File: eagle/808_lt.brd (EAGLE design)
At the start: 100 x 80 mm, 52 parts, among them IC1 TL071P, IC2 TL072P, Q1 2N3904, Q2 2N3906, Q3 2N3904, SW8 MSS42_SW_4PDT

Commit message: routing in low 90s
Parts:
- moved C74 26.7 mm to (7.62, 22.9), turned to 0 degrees
- moved R231 20.7 mm to (34.3, 15.2)
- moved R230 12.5 mm to (39.4, 24.1), turned to 0 degrees
- moved C81 12.0 mm to (78.7, 39.4), turned to 0 degrees
- moved R234 10.5 mm to (74.9, 44.5), turned to 180 degrees
- moved R215 10.2 mm to (33.0, 34.3)
- moved R214 9.92 mm to (25.4, 41.9), turned to 270 degrees
- moved R235 8.98 mm to (87.6, 31.8), turned to 90 degrees
- moved R227 8.03 mm to (43.2, 29.2)
- moved C73 6.35 mm to (33.0, 47.0)
- moved R211 5.24 mm to (21.6, 34.3)
- moved Q2 4.58 mm to (30.5, 40.6), turned to 0 degrees
- moved R216 4.02 mm to (17.8, 22.9)
- moved R219 3.81 mm to (24.1, 50.8)
- moved R229 2.84 mm to (44.5, 36.8)
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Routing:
- net GND: track 0.00 -> 254.7 mm
- net +15V: track 0.00 -> 166.3 mm
- net N$251: track 0.00 -> 138.5 mm
- net N$260: track 0.00 -> 74.7 mm
- net N$253: track 0.00 -> 44.2 mm
- net TRIG: track 0.00 -> 40.8 mm
- net N$264: track 0.00 -> 39.1 mm
- net N$259: track 0.00 -> 33.9 mm
- net N$262: track 0.00 -> 33.7 mm
- net N$273: track 0.00 -> 32.8 mm
- net N$39: track 0.00 -> 32.4 mm
- net N$263: track 0.00 -> 31.1 mm
- net LT: track 0.00 -> 30.9 mm
- net N$257: track 0.00 -> 29.6 mm
- net N$271: track 0.00 -> 22.1 mm
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
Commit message: closer
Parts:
- added OUT_NORM, PINK_NORM: 22-23-2021, con-molex:22-23-2021
- moved R223 31.9 mm to (36.8, 29.2)
- moved C74 26.9 mm to (33.0, 31.8), turned to 270 degrees
- moved R222 21.6 mm to (38.1, 20.3), turned to 90 degrees
- moved C81 18.2 mm to (71.1, 22.9), turned to 270 degrees
- moved R234 16.6 mm to (76.2, 27.9)
- moved C77 14.9 mm to (53.3, 27.9)
- moved C76 9.25 mm to (61.0, 50.8)
- moved R233 8.89 mm to (61.0, 26.7)
- moved C73 8.89 mm to (41.9, 47.0), turned to 0 degrees
- moved R219 8.52 mm to (31.8, 47.0)
- moved C78 8.03 mm to (55.9, 50.8)
- moved D56 8.03 mm to (48.3, 50.8)
- moved R228 8.03 mm to (58.4, 45.7)
- moved R214 7.73 mm to (33.0, 40.6)
- moved Q2 7.62 mm to (38.1, 40.6)
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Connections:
- new net N$3: OUTPUT.P$2, OUT_NORM.1
- new net N$4: PINK_NOISE.P$2, PINK_NORM.1
- net GND: now also OUT_NORM.2, PINK_NORM.2, SW8.P$12; no longer SW8.P$6
- net N$111: now also SW8.P$11; no longer SW8.P$5
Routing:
- net +15V: track 166.3 -> 50.2 mm
- net N$251: track 138.5 -> 31.8 mm
- net GND: track 254.7 -> 357.0 mm
- net -15V: track 2.54 -> 74.1 mm
- net N$264: track 39.1 -> 8.47 mm
- net N$260: track 74.7 -> 44.3 mm
- net N$259: track 33.9 -> 6.96 mm
- net N$273: track 32.8 -> 56.5 mm
- net N$256: track 9.72 -> 29.5 mm
- net N$253: track 44.2 -> 24.8 mm
- net N$111: track 0.00 -> 17.0 mm
- net N$271: track 22.1 -> 8.77 mm
- net N$262: track 33.7 -> 45.1 mm
- net N$257: track 29.6 -> 40.2 mm
- net N$250: track 18.3 -> 8.52 mm
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
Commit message: closer
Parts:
- moved R235 7.41 mm to (81.3, 31.8), turned to 180 degrees
- moved D56 3.81 mm to (48.3, 54.6)
- moved R226 3.81 mm to (49.5, 50.8)
- moved IC1 2.84 mm to (78.7, 38.1)
- moved R224 1.80 mm to (66.0, 34.3)
- moved R225 1.80 mm to (68.6, 45.7)
- moved R228 1.27 mm to (57.1, 45.7)
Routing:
- net GND: track 357.0 -> 0.00 mm
- net -15V: track 74.1 -> 0.00 mm
- net N$273: track 56.5 -> 0.00 mm
- net +15V: track 50.2 -> 0.00 mm
- net N$262: track 45.1 -> 0.00 mm
- net N$260: track 44.3 -> 0.00 mm
- net N$257: track 40.2 -> 0.00 mm
- net TRIG: track 38.3 -> 0.00 mm
- net N$251: track 31.8 -> 0.00 mm
- net N$256: track 29.5 -> 0.00 mm
- net N$263: track 29.2 -> 0.00 mm
- net N$39: track 28.6 -> 0.00 mm
- net LT: track 24.9 -> 0.00 mm
- net N$253: track 24.8 -> 0.00 mm
- net N$111: track 17.0 -> 0.00 mm
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
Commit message: 93 pct
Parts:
- moved C77 12.0 mm to (47.0, 38.1)
- moved R232 9.67 mm to (57.1, 25.4), turned to 180 degrees
- moved R227 6.35 mm to (49.5, 31.8)
- moved R229 5.39 mm to (50.8, 39.4), turned to 90 degrees
- moved R230 5.12 mm to (42.5, 19.1), turned to 90 degrees
- moved C83 4.02 mm to (69.8, 11.4), turned to 0 degrees
- moved R224 4.02 mm to (67.3, 38.1)
- moved C81 3.59 mm to (68.6, 25.4)
- moved R233 2.84 mm to (59.7, 29.2)
- moved C72 2.54 mm to (16.5, 34.3)
- moved IC1 2.54 mm to (78.7, 40.6)
- moved IC2 2.54 mm to (58.4, 39.4)
- moved R223 2.54 mm to (36.8, 31.8)
- moved C71 1.80 mm to (16.5, 25.4), turned to 90 degrees
- moved C75 1.27 mm to (39.4, 19.1)
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
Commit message: routed
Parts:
- moved R230 7.01 mm to (43.2, 26.0), turned to 0 degrees
- moved D56 4.58 mm to (44.5, 58.4), turned to 270 degrees
- moved C73 2.69 mm to (40.0, 48.9), turned to 90 degrees
- moved R226 1.80 mm to (48.3, 52.1)
- moved C75 1.27 mm to (40.6, 19.1)
- moved D55 1.27 mm to (21.6, 41.9), turned to 180 degrees
- moved R215 0.76 mm to (39.9, 34.3)
- moved C71 0.76 mm to (17.3, 25.4), turned to 180 degrees
- moved C72 0.51 mm to (17.0, 34.3)
- moved C77 0.25 mm to (47.2, 38.1)
- renumbered R3 to LEVEL, R4 to TUNE
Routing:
- net GND: track 0.00 -> 423.1 mm
- net +15V: track 0.00 -> 107.2 mm
- net N$262: track 0.00 -> 98.8 mm
- net N$251: track 0.00 -> 81.7 mm, vias 0 -> 4
- net -15V: track 0.00 -> 78.0 mm
- net TRIG: track 0.00 -> 56.5 mm
- net N$260: track 0.00 -> 43.0 mm
- net N$263: track 0.00 -> 35.2 mm
- net N$39: track 0.00 -> 32.7 mm
- net N$257: track 0.00 -> 32.4 mm
- net LT: track 0.00 -> 23.6 mm
- net N$111: track 0.00 -> 23.3 mm
- net N$271: track 0.00 -> 22.4 mm
- net N$253: track 0.00 -> 21.8 mm
- net N$267: track 0.00 -> 17.2 mm
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
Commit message: tweaks
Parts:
- moved R232 1.27 mm to (57.1, 26.7)
- moved SW8 1.27 mm to (52.1, 1.27)
- moved R230 0.51 mm to (42.7, 26.0)
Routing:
- net N$264: track 10.9 -> 8.96 mm
- net N$271: track 22.4 -> 24.1 mm
- net N$251: track 81.7 -> 83.0 mm
- net N$259: track 11.1 -> 9.85 mm
- net GND: track 423.1 -> 423.9 mm
- net N$111: track 23.3 -> 24.0 mm

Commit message: cutout
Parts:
- moved R229 0.57 mm to (51.1, 38.9)
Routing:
- net GND: track 423.9 -> 422.8 mm
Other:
- board size 100 x 80 mm -> 100 x 81 mm

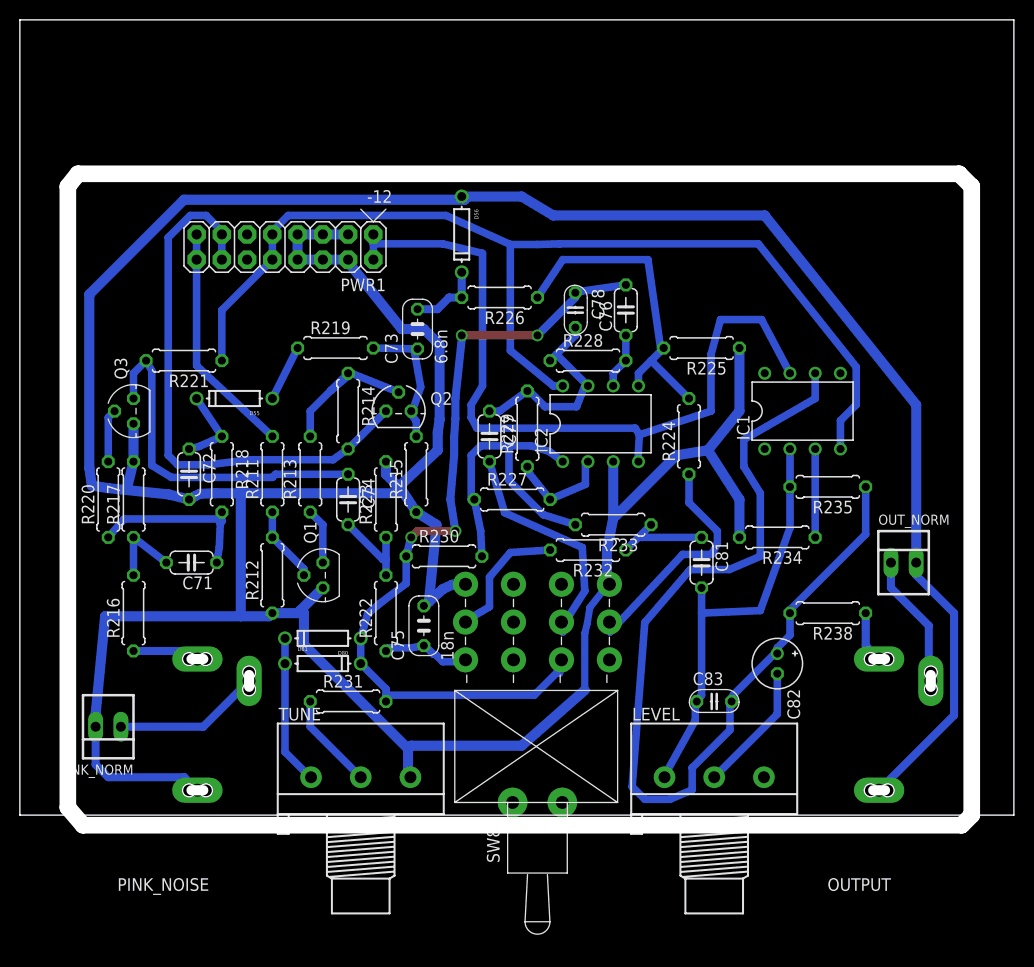
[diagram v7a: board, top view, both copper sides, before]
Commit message: thicker traces
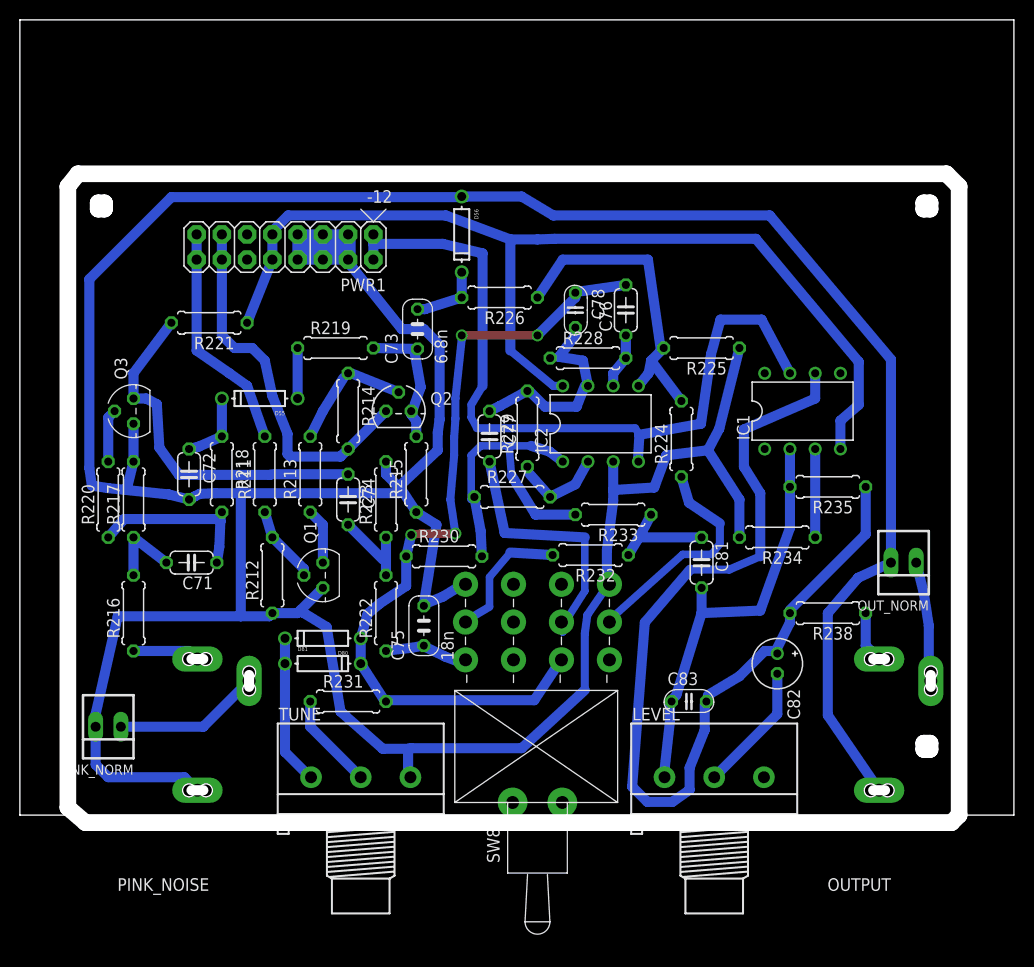
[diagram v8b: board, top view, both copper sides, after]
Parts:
- moved R221 4.58 mm to (19.1, 49.5)
- moved D55 2.54 mm to (24.1, 41.9)
- moved C83 2.54 mm to (67.3, 11.4)
- moved R233 1.02 mm to (59.7, 30.2)
- moved R224 0.80 mm to (66.5, 37.8)
- moved R211 0.76 mm to (24.6, 34.3)
- moved R232 0.57 mm to (57.4, 26.2)
- moved R227 0.25 mm to (49.5, 32.0)
- moved R228 0.25 mm to (57.1, 46.0)
- turned OUT_NORM to 180 degrees
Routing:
- net TRIG: track 56.0 -> 37.2 mm
- net +15V: track 107.2 -> 102.9 mm
- net N$271: track 24.1 -> 26.6 mm
- net N$241: track 15.8 -> 13.5 mm
- net N$3: track 13.6 -> 12.1 mm
- net N$262: track 99.0 -> 100.3 mm
- net N$111: track 24.0 -> 22.9 mm
- net N$256: track 10.5 -> 9.32 mm
- net N$259: track 9.85 -> 10.9 mm
- net N$263: track 35.2 -> 36.2 mm
- net N$268: track 8.13 -> 7.36 mm
- net N$248: track 5.68 -> 5.08 mm
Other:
- board size 100 x 81 mm -> 100 x 80.8 mm
